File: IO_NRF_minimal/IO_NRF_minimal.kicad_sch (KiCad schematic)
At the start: 30 parts, among them J1 12V_IN, J2 Programmer_Pins_SPI, J3 XKC-Y2S-IN, J4 External_Inputs_Terminal, U1 NRF24L01_Breakout, U2 AP7370-33WW-7, U3 ATtiny84-20SS, U4 TLP291

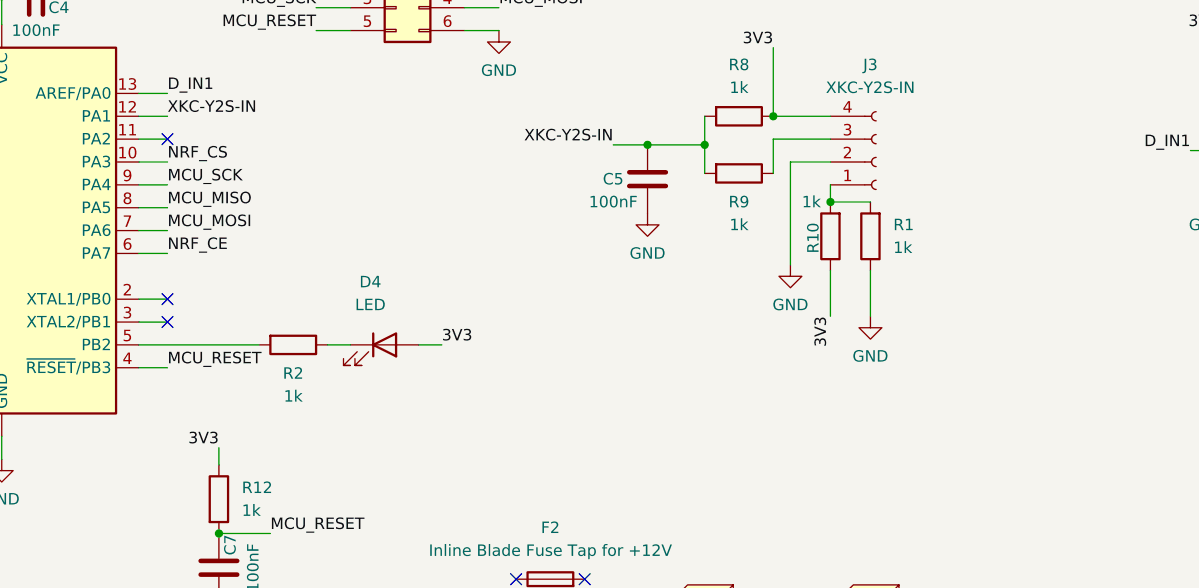
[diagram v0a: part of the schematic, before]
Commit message: Updated both PCBs with TEMT6000 and XKC enabler
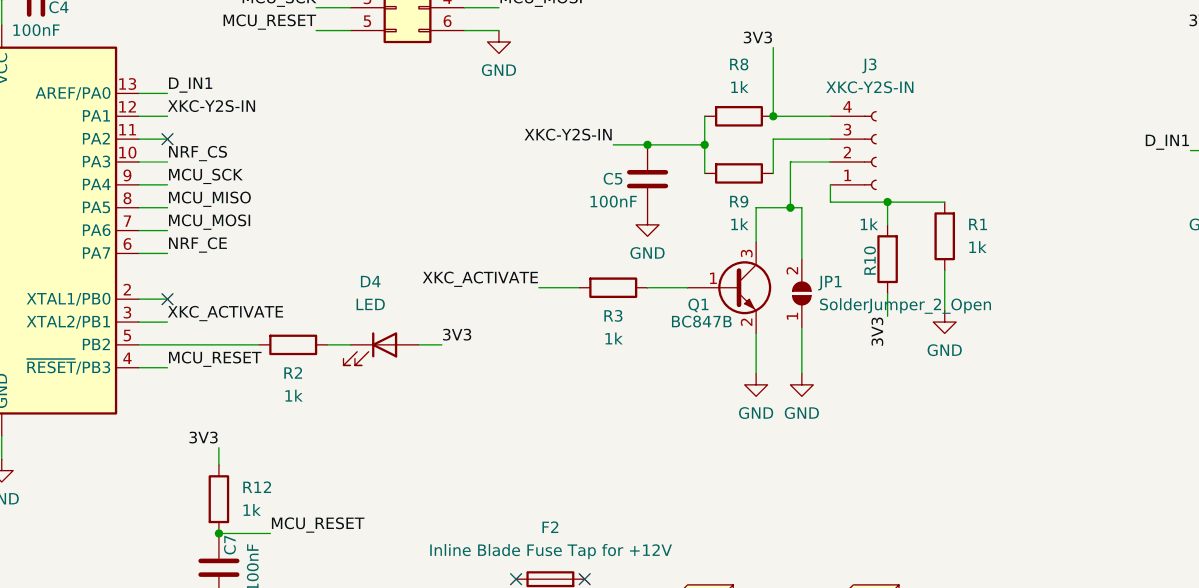
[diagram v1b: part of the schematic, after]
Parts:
- added JP1: SolderJumper_2_Open, Jumper:SolderJumper-2_P1.3mm_Open_RoundedPad1.0x1.5mm, symbol Jumper:SolderJumper_2_Open
- added Q1: BC847B, Package_TO_SOT_SMD:SOT-23, symbol Device:Q_NPN_BEC
- added R3: 1k, Resistor_SMD:R_0805_2012Metric, symbol Device:R
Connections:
- net GND: now also JP1.1 (A), Q1.2 (E); no longer J3.2 (Pin_2)
- net XKC_ACTIVATE: now reaches U3.3 (XTAL2/PB1)
- net XKC_ACTIVATE: now also R3.2
- new net: J3.2 (Pin_2), JP1.2 (B), Q1.3 (C)
- new net: Q1.1 (B), R3.1
- no-connect marks 8 -> 7
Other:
- moved on the sheet: R1, R10

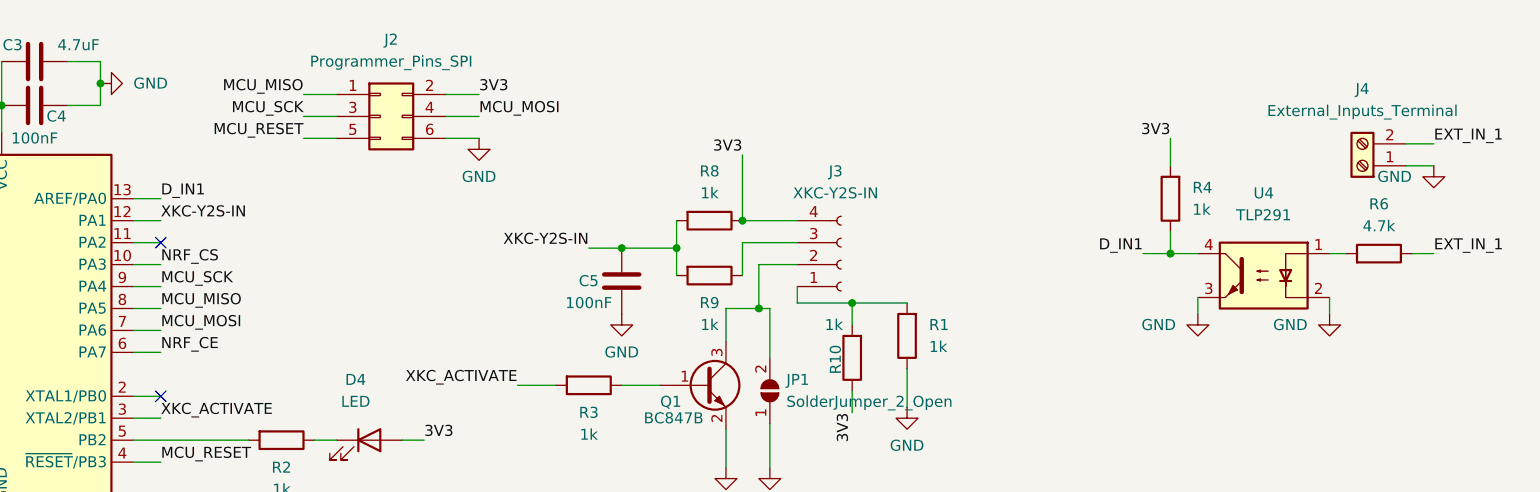
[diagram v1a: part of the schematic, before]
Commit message: Minimalized IO-NRF, no Digital Input
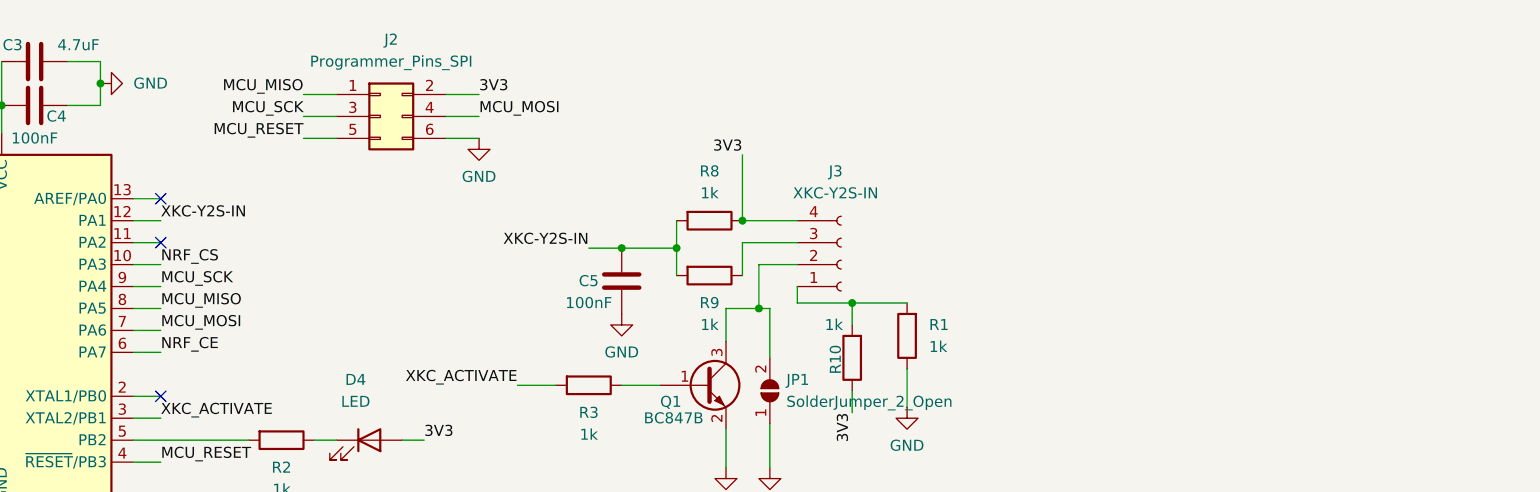
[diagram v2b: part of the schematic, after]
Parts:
- removed J4: External_Inputs_Terminal, my_kicad:SORKAPOCS-3.5mm-2, symbol Connector:Screw_Terminal_01x02
- removed R4: 1k, Resistor_SMD:R_0805_2012Metric, symbol Device:R
- removed R6: 4.7k, Resistor_SMD:R_0805_2012Metric, symbol Device:R
- removed U4: TLP291, Package_SO:SOIC-4_4.55x2.6mm_P1.27mm, symbol Isolator:TLP291
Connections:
- net D_IN1: no longer names the net of U3.13 (AREF/PA0)
- no-connect marks 7 -> 8

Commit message: Updated BOMs, manufacturing (beültetés árak) and PCBs
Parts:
- removed C2: 47uF, Capacitor_SMD:CP_Elec_6.3x5.4, symbol Device:C_Polarized
- added C2: 10uF, Capacitor_SMD:C_1210_3225Metric, symbol Device:C
- C6: value C_Polarized -> 100uF
- X1: renamed from N1; value Housing -> G1013B (GAI)
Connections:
- net 3V3: now also C2.1
- net GND: now also C2.2
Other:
- note removed: "G1020B - doboz Lomex"
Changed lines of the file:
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@@
     (stroke (width 0) (type default) (color 0 0 0 0))
-  )
-  (text "G1020B - doboz Lomex\n" (at 19.685 80.645 0)
-    (effects (font (size 3 3)) (justify left bottom))
   )
   (label "MCU_RESET" (at 133.35 26.67 180)
@@
   (symbol (lib_id "Mechanical:Housing") (at 176.53 92.075 0) (unit 1)
     (in_bom yes) (on_board yes) (fields_autoplaced)
-    (property "Reference" "N1" (id 0) (at 180.34 91.1224 0)
-      (effects (font (size 1.27 1.27)) (justify left))
-    )
-    (property "Value" "Housing" (id 1) (at 180.34 93.6624 0)
+    (property "Reference" "X1" (id 0) (at 180.34 91.1224 0)
+      (effects (font (size 1.27 1.27)) (justify left))
+    )
+    (property "Value" "G1013B (GAI)" (id 1) (at 180.34 93.6624 0)
       (effects (font (size 1.27 1.27)) (justify left))
     )
@@
       (effects (font (size 1.27 1.27)) (justify left))
     )
-    (property "Value" "C_Polarized" (id 1) (at 36.83 56.515 0)
+    (property "Value" "100uF" (id 1) (at 36.83 56.515 0)
       (effects (font (size 1.27 1.27)) (justify left))
     )
@@
     (pin "4")
   )
+  (symbol (lib_id "Device:C") (at 80.01 118.745 90) (unit 1)
+    (in_bom yes) (on_board yes) (fields_autoplaced)
+    (property "Reference" "C2" (id 0) (at 80.01 111.76 90))
+    (property "Value" "10uF" (id 1) (at 80.01 114.3 90))
+    (property "Footprint" "Capacitor_SMD:C_1210_3225Metric" (id 2) (at 83.82 117.7798 0)
+      (effects (font (size 1.27 1.27)) hide)
+    )
+    (property "Datasheet" "~" (id 3) (at 80.01 118.745 0)
+      (effects (font (size 1.27 1.27)) hide)
+    )
+    (property "LOMEX" "82-08-34" (id 4) (at 80.01 118.745 0)
+      (effects (font (size 1.27 1.27)) hide)
+    )
+    (pin "1")
+    (pin "2")
+  )
   (symbol (lib_id "Device:R") (at 122.555 78.74 0) (unit 1)
     (in_bom yes) (on_board yes) (fields_autoplaced)
@@
     (pin "2")
   )
-  (symbol (lib_id "Device:C_Polarized") (at 80.01 118.745 90) (unit 1)
-    (in_bom yes) (on_board yes) (fields_autoplaced)
-    (property "Reference" "C2" (id 0) (at 79.121 123.19 90))
-    (property "Value" "47uF" (id 1) (at 79.121 125.73 90))
-    (property "Footprint" "Capacitor_SMD:CP_Elec_6.3x5.4" (id 2) (at 83.82 117.7798 0)
-      (effects (font (size 1.27 1.27)) hide)
-    )
-    (property "Datasheet" "~" (id 3) (at 80.01 118.745 0)
-      (effects (font (size 1.27 1.27)) hide)
-    )
-    (property "LOMEX" "91-00-88 " (id 4) (at 80.01 118.745 0)
-      (effects (font (size 1.27 1.27)) hide)
-    )
-    (pin "1")
-    (pin "2")
-  )
   (symbol (lib_id "power:GND") (at 58.42 113.03 0) (unit 1)
     (in_bom yes) (on_board yes)
@@
       (reference "C1") (unit 1) (value "10uF") (footprint "Capacitor_SMD:C_1210_3225Metric")
     )
-    (path "/b06ead61-1750-4e8c-a8f2-3bfa668f7005"
-      (reference "C2") (unit 1) (value "47uF") (footprint "Capacitor_SMD:CP_Elec_6.3x5.4")
+    (path "/8b5be057-974f-40de-b23c-8d62554b1c53"
+      (reference "C2") (unit 1) (value "10uF") (footprint "Capacitor_SMD:C_1210_3225Metric")
     )
     (path "/e90bdb1e-bec8-4126-8679-7f4df5781ec1"
@@
     )
     (path "/7bdf696d-e4c2-4f69-a919-2ca4889ca97a"
-      (reference "C6") (unit 1) (value "C_Polarized") (footprint "Capacitor_SMD:CP_Elec_5x5.3")
+      (reference "C6") (unit 1) (value "100uF") (footprint "Capacitor_SMD:CP_Elec_5x5.3")
     )
     (path "/c207590d-b044-46bd-8b35-03394f2c3802"
@@
       (reference "JP1") (unit 1) (value "SolderJumper_2_Open") (footprint "Jumper:SolderJumper-2_P1.3mm_Open_RoundedPad1.0x1.5mm")
     )
-    (path "/42bf9880-3dea-4d00-81a9-64231cc325ad"
-      (reference "N1") (unit 1) (value "Housing") (footprint "")
-    )
     (path "/f61d86f7-ac9f-480e-87c7-aebed30ce7b8"
       (reference "N2") (unit 1) (value "XKC-Y25-NPN") (footprint "")
@@
       (reference "U3") (unit 1) (value "ATtiny84-20SS") (footprint "Package_SO:SOIC-14_3.9x8.7mm_P1.27mm")
     )
-  )
+    (path "/42bf9880-3dea-4d00-81a9-64231cc325ad"
+      (reference "X1") (unit 1) (value "G1013B (GAI)") (footprint "")
+    )
+  )

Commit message: latest versions
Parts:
- removed U1: NRF24L01_Breakout, mykicad_6:NRF24L01_SMD, symbol RF:NRF24L01_Breakout
- added U1: NRF24L01_SMD, mykicad_6:NRF24L01_SMD, symbol MY_KiCad_6:NRF24L01_SMD
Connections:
- net 3V3: now also U1.1 (3V3)
- net GND: now also U1.2 (GND)
- net MCU_MISO: now also U1.6 (MOSI)
- net MCU_MOSI: now also U1.7 (MISO)
- net MCU_SCK: now also U1.5 (SCK)
- net NRF_CE: now also U1.3 (CE)
- net NRF_CS: now also U1.4 (CSN)
- no-connect marks 8 -> 9
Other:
- moved on the sheet: C6, C8
